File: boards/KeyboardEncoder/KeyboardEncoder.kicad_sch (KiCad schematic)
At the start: 2 parts

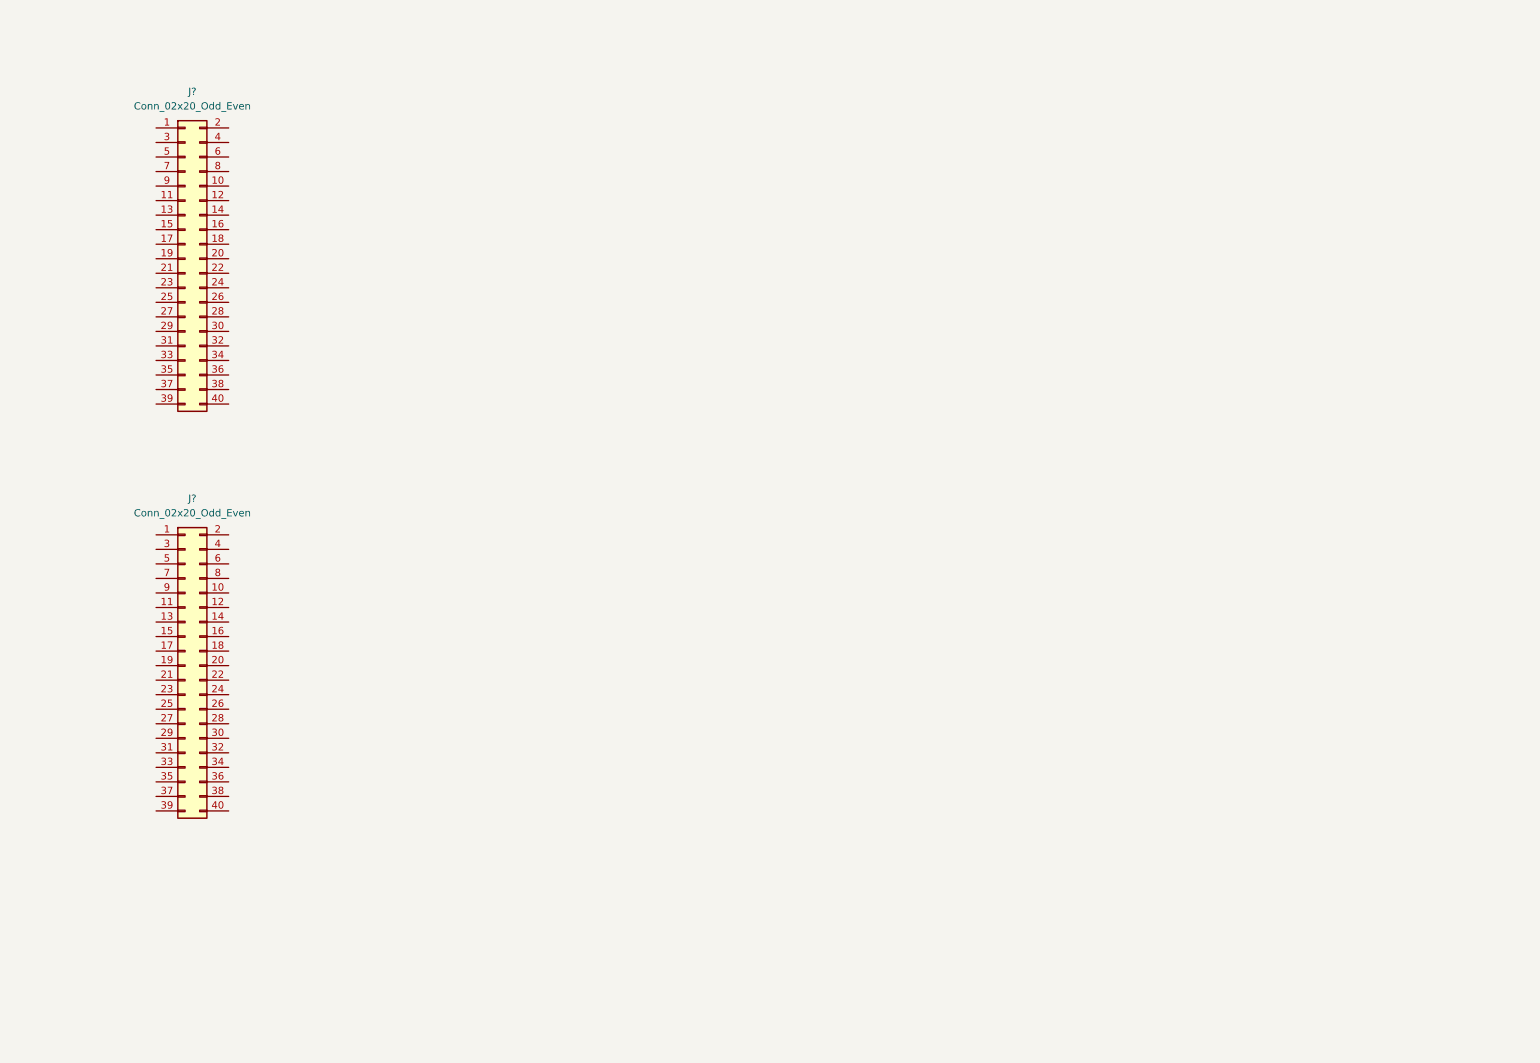
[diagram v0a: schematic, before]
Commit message: Added Keyboard encoder and Midi encoder design using shift registers
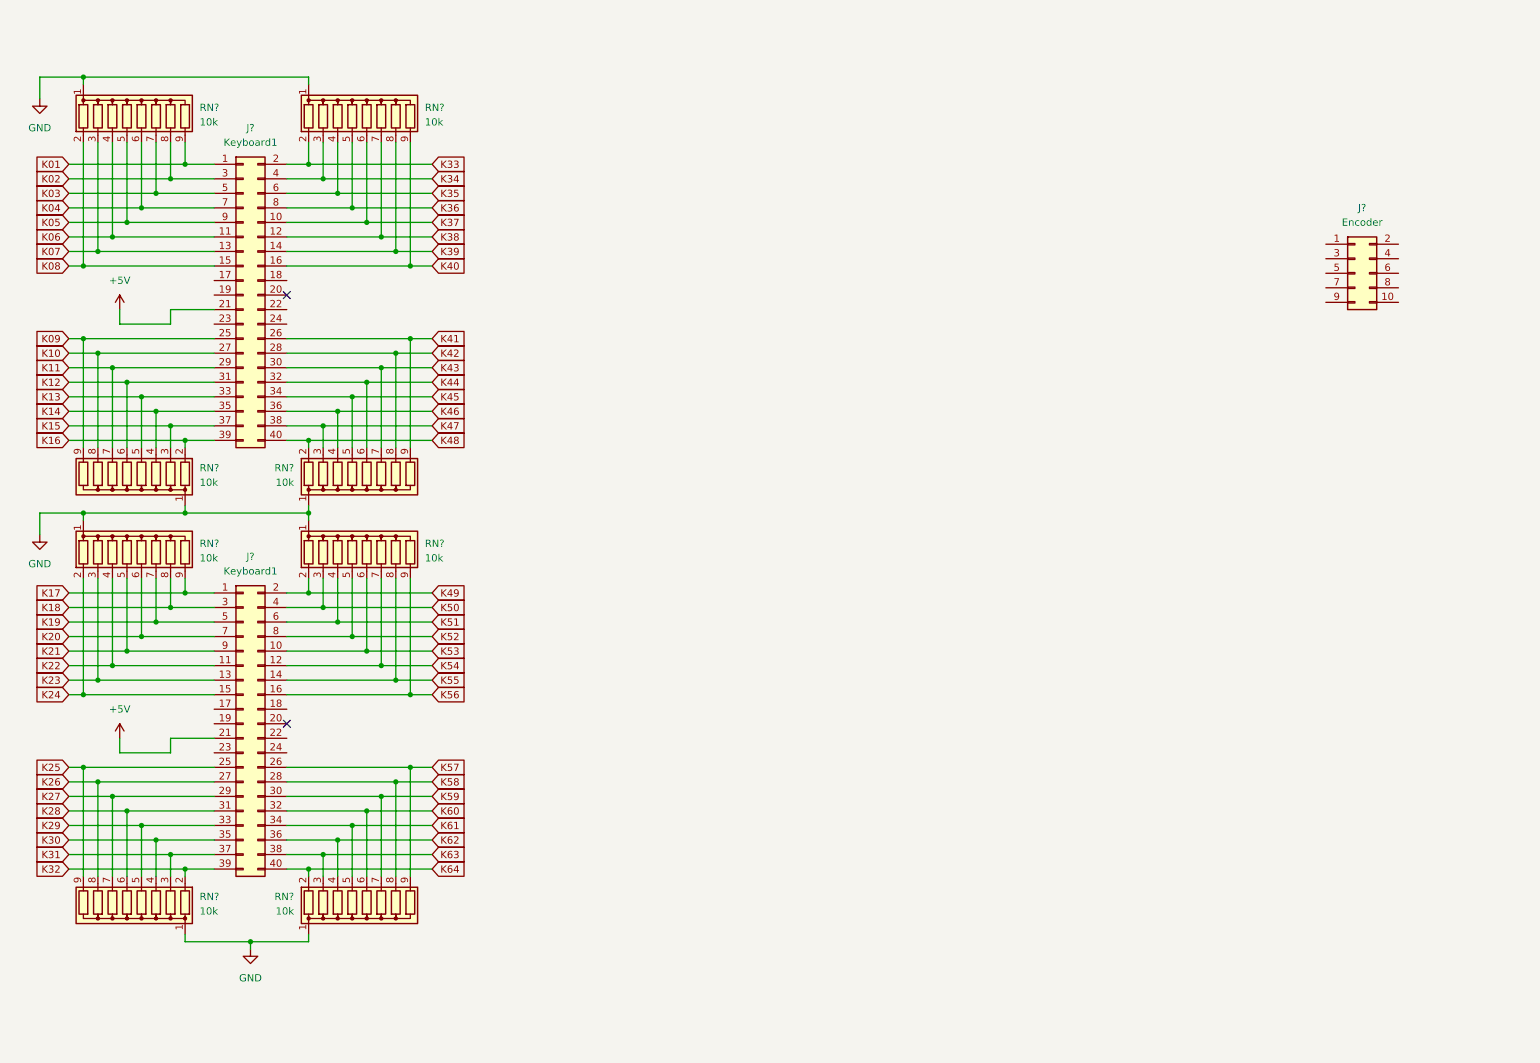
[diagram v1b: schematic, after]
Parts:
- removed J? (x2): Conn_02x20_Odd_Even, symbol Connector_Generic:Conn_02x20_Odd_Even
- added J? (x2): Keyboard1, symbol Connector_Generic:Conn_02x20_Odd_Even
- added J?: Encoder, symbol Connector_Generic:Conn_02x05_Odd_Even
- added RN? (x8): 10k, Resistor_THT:R_Array_SIP9, symbol Device:R_Network08
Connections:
- new net +5V: J?.21 (Pin_21), J?.21 (Pin_21)
- new net GND: RN?.1 (common), RN?.1 (common), RN?.1 (common), RN?.1 (common), RN?.1 (common), RN?.1 (common), RN?.1 (common), RN?.1 (common)
- new net K01: J?.1 (Pin_1), RN?.9 (R8)
- new net K02: J?.3 (Pin_3), RN?.8 (R7)
- new net K03: J?.5 (Pin_5), RN?.7 (R6)
- new net K04: J?.7 (Pin_7), RN?.6 (R5)
- new net K05: J?.9 (Pin_9), RN?.5 (R4)
- new net K06: J?.11 (Pin_11), RN?.4 (R3)
- new net K07: J?.13 (Pin_13), RN?.3 (R2)
- new net K08: J?.15 (Pin_15), RN?.2 (R1)
- new net K09: J?.25 (Pin_25), RN?.9 (R8)
- new net K10: J?.27 (Pin_27), RN?.8 (R7)
- new net K11: J?.29 (Pin_29), RN?.7 (R6)
- new net K12: J?.31 (Pin_31), RN?.6 (R5)
- new net K13: J?.33 (Pin_33), RN?.5 (R4)
- new net K14: J?.35 (Pin_35), RN?.4 (R3)
- new net K15: J?.37 (Pin_37), RN?.3 (R2)
- new net K16: J?.39 (Pin_39), RN?.2 (R1)
- new net K17: J?.1 (Pin_1), RN?.9 (R8)
- new net K18: J?.3 (Pin_3), RN?.8 (R7)
- new net K19: J?.5 (Pin_5), RN?.7 (R6)
- new net K20: J?.7 (Pin_7), RN?.6 (R5)
- new net K21: J?.9 (Pin_9), RN?.5 (R4)
- new net K22: J?.11 (Pin_11), RN?.4 (R3)
- new net K23: J?.13 (Pin_13), RN?.3 (R2)
- new net K24: J?.15 (Pin_15), RN?.2 (R1)
- new net K25: J?.25 (Pin_25), RN?.9 (R8)
- new net K26: J?.27 (Pin_27), RN?.8 (R7)
- new net K27: J?.29 (Pin_29), RN?.7 (R6)
- new net K28: J?.31 (Pin_31), RN?.6 (R5)
- new net K29: J?.33 (Pin_33), RN?.5 (R4)
- new net K30: J?.35 (Pin_35), RN?.4 (R3)
- new net K31: J?.37 (Pin_37), RN?.3 (R2)
- new net K32: J?.39 (Pin_39), RN?.2 (R1)
- new net K33: J?.2 (Pin_2), RN?.2 (R1)
- new net K34: J?.4 (Pin_4), RN?.3 (R2)
- new net K35: J?.6 (Pin_6), RN?.4 (R3)
- new net K36: J?.8 (Pin_8), RN?.5 (R4)
- new net K37: J?.10 (Pin_10), RN?.6 (R5)
- new net K38: J?.12 (Pin_12), RN?.7 (R6)
- new net K39: J?.14 (Pin_14), RN?.8 (R7)
- new net K40: J?.16 (Pin_16), RN?.9 (R8)
- new net K41: J?.26 (Pin_26), RN?.9 (R8)
- new net K42: J?.28 (Pin_28), RN?.8 (R7)
- new net K43: J?.30 (Pin_30), RN?.7 (R6)
- new net K44: J?.32 (Pin_32), RN?.6 (R5)
- new net K45: J?.34 (Pin_34), RN?.5 (R4)
- new net K46: J?.36 (Pin_36), RN?.4 (R3)
- new net K47: J?.38 (Pin_38), RN?.3 (R2)
- new net K48: J?.40 (Pin_40), RN?.2 (R1)
- new net K49: J?.2 (Pin_2), RN?.2 (R1)
- new net K50: J?.4 (Pin_4), RN?.3 (R2)
- new net K51: J?.6 (Pin_6), RN?.4 (R3)
- new net K52: J?.8 (Pin_8), RN?.5 (R4)
- new net K53: J?.10 (Pin_10), RN?.6 (R5)
- new net K54: J?.12 (Pin_12), RN?.7 (R6)
- new net K55: J?.14 (Pin_14), RN?.8 (R7)
- new net K56: J?.16 (Pin_16), RN?.9 (R8)
- new net K57: J?.26 (Pin_26), RN?.9 (R8)
- new net K58: J?.28 (Pin_28), RN?.8 (R7)
- new net K59: J?.30 (Pin_30), RN?.7 (R6)
- new net K60: J?.32 (Pin_32), RN?.6 (R5)
- new net K61: J?.34 (Pin_34), RN?.5 (R4)
- new net K62: J?.36 (Pin_36), RN?.4 (R3)
- new net K63: J?.38 (Pin_38), RN?.3 (R2)
- new net K64: J?.40 (Pin_40), RN?.2 (R1)
- no-connect marks 0 -> 2

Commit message: Updated keyboard encoder to use 8-1 Mux instead of shift registers
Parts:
- removed J?: Encoder, symbol Connector_Generic:Conn_02x05_Odd_Even
- added J3: Encoder, symbol Connector_Generic:Conn_02x08_Odd_Even
- added U1, U10, U2, U3, U4, U6, U7, U9: 74151, symbol 74xx_IEEE:74151
- added U5: ULN2803A, symbol Transistor_Array:ULN2803A
- added U8: 4069, symbol 4xxx:4069
- gave numbers to parts that had none: 10
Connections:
- net +5V: now also J3.2 (Pin_2), J3.4 (Pin_4), U1.16 (VCC), U10.16 (VCC), U2.16 (VCC), U3.16 (VCC), U4.16 (VCC), U5.10 (COM), U6.16 (VCC), U7.16 (VCC), U9.16 (VCC)
- net GND: now also J3.14 (Pin_14), J3.16 (Pin_16), U1.8 (GND), U10.8 (GND), U2.8 (GND), U3.8 (GND), U4.8 (GND), U5.9 (GND), U6.8 (GND), U7.8 (GND), U8.11, U8.13, U9.8 (GND)
- net K01: now also U1.4 (I0)
- net K02: now also U1.3 (I1)
- net K03: now also U1.2 (I2)
- net K04: now also U1.1 (I3)
- net K05: now also U1.15 (I4)
- net K06: now also U1.14 (I5)
- net K07: now also U1.13 (I6)
- net K08: now also U1.12 (I7)
- net K09: now also U2.4 (I0)
- net K10: now also U2.3 (I1)
- net K11: now also U2.2 (I2)
- net K12: now also U2.1 (I3)
- net K13: now also U2.15 (I4)
- net K14: now also U2.14 (I5)
- net K15: now also U2.13 (I6)
- net K16: now also U2.12 (I7)
- net K17: now also U3.4 (I0)
- net K18: now also U3.3 (I1)
- net K19: now also U3.2 (I2)
- net K20: now also U3.1 (I3)
- net K21: now also U3.15 (I4)
- net K22: now also U3.14 (I5)
- net K23: now also U3.13 (I6)
- net K24: now also U3.12 (I7)
- net K25: now also U4.4 (I0)
- net K26: now also U4.3 (I1)
- net K27: now also U4.2 (I2)
- net K28: now also U4.1 (I3)
- net K29: now also U4.15 (I4)
- net K30: now also U4.14 (I5)
- net K31: now also U4.13 (I6)
- net K32: now also U4.12 (I7)
- net K33: now also U6.4 (I0)
- net K34: now also U6.3 (I1)
- net K35: now also U6.2 (I2)
- net K36: now also U6.1 (I3)
- net K37: now also U6.15 (I4)
- net K38: now also U6.14 (I5)
- net K39: now also U6.13 (I6)
- net K40: now also U6.12 (I7)
- net K41: now also U7.4 (I0)
- net K42: now also U7.3 (I1)
- net K43: now also U7.2 (I2)
- net K44: now also U7.1 (I3)
- net K45: now also U7.15 (I4)
- net K46: now also U7.14 (I5)
- net K47: now also U7.13 (I6)
- net K48: now also U7.12 (I7)
- net K49: now also U9.4 (I0)
- net K50: now also U9.3 (I1)
- net K51: now also U9.2 (I2)
- net K52: now also U9.1 (I3)
- net K53: now also U9.15 (I4)
- net K54: now also U9.14 (I5)
- net K55: now also U9.13 (I6)
- net K56: now also U9.12 (I7)
- net K57: now also U10.4 (I0)
- net K58: now also U10.3 (I1)
- net K59: now also U10.2 (I2)
- net K60: now also U10.1 (I3)
- net K61: now also U10.15 (I4)
- net K62: now also U10.14 (I5)
- net K63: now also U10.13 (I6)
- net K64: now also U10.12 (I7)
- new net: J3.15 (Pin_15), U5.11 (O8)
- new net: J3.13 (Pin_13), U5.12 (O7)
- new net: J3.11 (Pin_11), U5.13 (O6)
- new net: J3.9 (Pin_9), U5.14 (O5)
- new net: J3.7 (Pin_7), U5.15 (O4)
- new net: J3.5 (Pin_5), U5.16 (O3)
- new net: J3.3 (Pin_3), U5.17 (O2)
- new net: J3.1 (Pin_1), U5.18 (O1)
- new net: J3.10 (Pin_10), U8.5
- new net: J3.12 (Pin_12), U8.9
- new net: J3.6 (Pin_6), U8.1
- new net: J3.8 (Pin_8), U8.3
- new net En: U1.7 (~{E}), U10.7 (~{E}), U2.7 (~{E}), U3.7 (~{E}), U4.7 (~{E}), U6.7 (~{E}), U7.7 (~{E}), U8.2, U9.7 (~{E})
- new net O1: U1.5 (Q), U5.1 (I1)
- new net O2: U2.5 (Q), U5.2 (I2)
- new net O3: U3.5 (Q), U5.3 (I3)
- new net O4: U4.5 (Q), U5.4 (I4)
- new net O5: U5.5 (I5), U6.5 (Q)
- new net O6: U5.6 (I6), U7.5 (Q)
- new net O7: U5.7 (I7), U9.5 (Q)
- new net O8: U10.5 (Q), U5.8 (I8)
- new net S0: U1.11 (S0), U10.11 (S0), U2.11 (S0), U3.11 (S0), U4.11 (S0), U6.11 (S0), U7.11 (S0), U8.4, U9.11 (S0)
- new net S1: U1.10 (S1), U10.10 (S1), U2.10 (S1), U3.10 (S1), U4.10 (S1), U6.10 (S1), U7.10 (S1), U8.6, U9.10 (S1)
- new net S2: U1.9 (S2), U10.9 (S2), U2.9 (S2), U3.9 (S2), U4.9 (S2), U6.9 (S2), U7.9 (S2), U8.8, U9.9 (S2)
- no-connect marks 2 -> 24
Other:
- added sheet Power Pins (PowerPins.kicad_sch)
